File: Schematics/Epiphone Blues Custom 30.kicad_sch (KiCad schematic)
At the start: 274 parts, among them J3 Conn_Coaxial_Power, M1 Fan, SW2 EQ mode, SW3 POWER, SW4 STANDBY, SW5 PENTODE

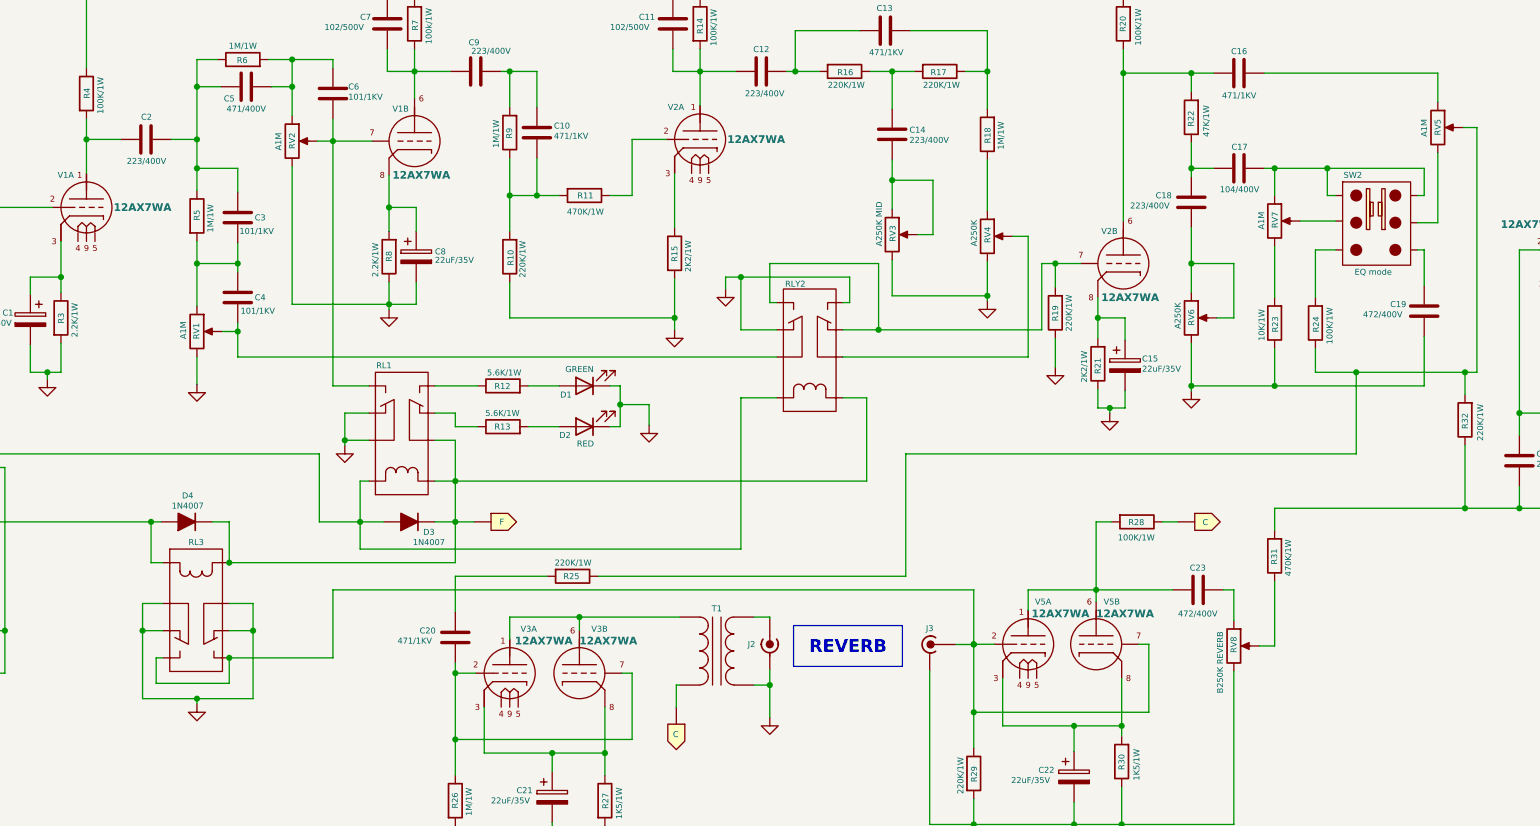
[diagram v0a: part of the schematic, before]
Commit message: Added text to schematic
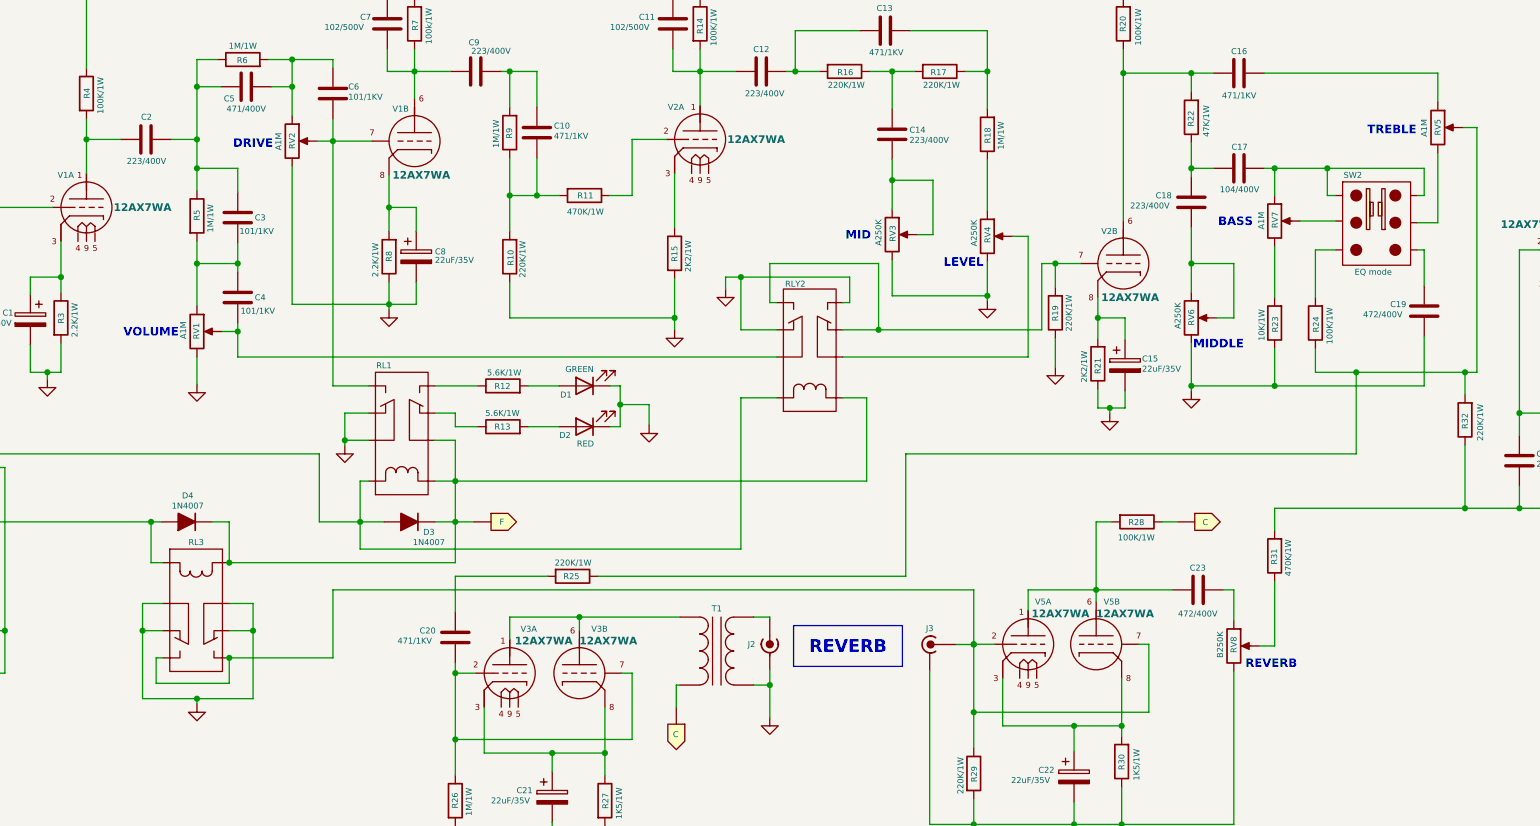
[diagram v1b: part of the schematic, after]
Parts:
- RV3: value A250K MID -> A250K
- RV8: value B250K REVERB -> B250K
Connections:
- net at FCR.: now also B., C33.1, R49.1; no longer TRF4.
- net at SS1.: now also F4.1; no longer SW4.
- net at 0VAC.: now also TR2.; no longer PT3.
- net at 60VAC.: now also TR2.; no longer PT11.
- net at PT2.: now also PT3., PT6. (x2)
- net at V7.: now also C29.1, R44.2, V6.
- net at PT5.: now also PT6. (x2)
- net at PT6.: no longer PT5. (x2)
- net at PT4.: now also PT1., PT7.
- net at ff.: now also BLUE.; no longer TR3.
- net at BLUE.: now also OT6.; no longer ff.
- net at PT7.: now also PT1.
- net at PT1.: no longer PT7.
- net at U?.: now also OUT1.; no longer TR3.
- net at OUT1.: now also PS1., V6.; no longer U?.
- net at 120VAC.: now also TR2.; no longer PT5.
- net at TR3.: now also d.; no longer d.
- net at a.: now also d.; no longer TR3.
- net at s.: now also d.; no longer TR3.
- net at d.: now also s.; no longer TR3.
- net at PT7.: now also 100VAC.
- net at 100VAC.: now also TR2.; no longer PT7.
- net at 5VAC.: now also PT13.
- net at PT13.: now also C35.1, HTFS., R50.1, V8.; no longer 5VAC.
- net at BLK.: now also SW3.; no longer PT1.
- net at SW3.: now also BLU.; no longer BLK.
- net at 0VAC.: now also TR2.; no longer PT6.
- net at 100VAC.: now also TR2.; no longer PT4.
- net at V6., V7.: now also PT15.; no longer PT14.
- net at PT1.: now also PT8.
- net at PT8.: no longer PT1.
- net at SW2.: now also RV7.; no longer RV5.
- net at RV7.: now also R23.2; no longer SW2.
- net at 120VAC.: now also TR2.; no longer PT8.
- net at SW4.: now also 350VAC.; no longer 350VAC.
- net at 350VAC.: now also TR2.; no longer SW4.
- net at PT2.: now also PT3.
- net at PT3.: no longer PT2.
- net at PT5.: now also PT1., PT8.
- net at 0VAC.: now also PT12.
- net at PT12.: now also F7.1; no longer 0VAC.
- net at s.: now also a.; no longer d.
- net at a.: now also J6., J7.; no longer s.
- net at BRN.: now also F9.2; no longer SW3.
- net at BLU.: now also AC-Input1.; no longer SW3.
- net at PT3.: now also PT2.
- net at PT2.: no longer PT3.
- new net: C3.1, D6.1 (K), D7.1 (K), F., M1. (-), V1., V2., V3., V4., V5.
- new net: FCR., TRF4.
- new net: SS1., SW4.
- new net: 0VAC., PT3.
- new net: 0VAC., TR2. (x2)
- new net: D4.2 (A), J4., RL3.
- new net: D3.2 (A), J4., RL1., RLY2.
- new net: J4., PB1.
- new net: 60VAC., PT11.
- new net: J3. (In), R29.1, RL3., V5A., V5B.
- new net: OUT2., PS2., V7.
- new net: TR3., ff.
- new net: TR3., U?.
- new net: B., PS5., PS6.
- new net: J5., J6., J7., J8., J9., d.
- new net: C4.2, RLY2., RV1.
- new net: 120VAC., PT5.
- new net: R19.2, RLY2., V2B.
- new net: RLY2., RV4.
- new net: TR3., d.
- new net: TR3., a.
- new net: TR3., s.
- new net: BLK., PT1.
- new net: 0VAC., PT6.
- new net: 100VAC., PT4.
- new net: PT14., V6., V7.
- new net: C17.2, RV7., SW2.
- new net: RV5., SW2.
- new net: 120VAC., PT8.
- new net: 350VAC., SW4.
- new net: C6.2, RL1., RV2., V1B.
- new net: BRN., SW3.
- new net: J2. (In), T1. (SB)
- now unconnected: PT1., PT1., PT3., PT3., PT6., PT6., PT7., PT8., V6., V6.
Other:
- note added: "BASS"
- note added: "DRIVE"
- note added: "LEVEL"
- note added: "MID"
- note added: "MIDDLE"
- note added: "TREBLE"
- note added: "VOLUME"
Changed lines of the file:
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@@
 		)
 	)
+	(text "TREBLE"
+		(exclude_from_sim no)
+		(at 281.178 44.958 0)
+		(effects
+			(font
+				(size 1.27 1.27)
+				(thickness 0.254)
+				(bold yes)
+				(color 0 132 0 1)
+			)
+		)
+	)
+	(text "MID"
+		(exclude_from_sim no)
+		(at 201.422 60.706 0)
+		(effects
+			(font
+				(size 1.27 1.27)
+				(thickness 0.254)
+				(bold yes)
+				(color 0 132 0 1)
+			)
+		)
+	)
 	(text "RED"
 		(exclude_from_sim no)
@@
 		)
 	)
+	(text "DRIVE"
+		(exclude_from_sim no)
+		(at 110.998 46.99 0)
+		(effects
+			(font
+				(size 1.27 1.27)
+				(thickness 0.254)
+				(bold yes)
+				(color 0 132 0 1)
+			)
+		)
+	)
 	(text "BRN"
 		(exclude_from_sim no)
@@
 		)
 	)
+	(text "MIDDLE"
+		(exclude_from_sim no)
+		(at 255.27 76.962 0)
+		(effects
+			(font
+				(size 1.27 1.27)
+				(thickness 0.254)
+				(bold yes)
+				(color 0 132 0 1)
+			)
+		)
+	)
 	(text "MAIN FUSE\n100-120VAC T3.15AL 250V\n220-240VAC T1.6AL 250V"
 		(exclude_from_sim no)
@@
 		)
 	)
+	(text "VOLUME"
+		(exclude_from_sim no)
+		(at 95.758 75.184 0)
+		(effects
+			(font
+				(size 1.27 1.27)
+				(thickness 0.254)
+				(bold yes)
+				(color 0 132 0 1)
+			)
+		)
+	)
 	(text "BLU"
 		(exclude_from_sim no)
@@
 		)
 	)
+	(text "BASS"
+		(exclude_from_sim no)
+		(at 257.81 58.674 0)
+		(effects
+			(font
+				(size 1.27 1.27)
+				(thickness 0.254)
+				(bold yes)
+				(color 0 132 0 1)
+			)
+		)
+	)
 	(text "@250mA"
 		(exclude_from_sim no)
@@
 		)
 	)
+	(text "REVERB"
+		(exclude_from_sim no)
+		(at 263.144 124.714 0)
+		(effects
+			(font
+				(size 1.27 1.27)
+				(thickness 0.254)
+				(bold yes)
+				(color 0 132 0 1)
+			)
+		)
+	)
 	(text "BLK"
 		(exclude_from_sim no)
@@
 		)
 	)
+	(text "LEVEL"
+		(exclude_from_sim no)
+		(at 217.17 64.77 0)
+		(effects
+			(font
+				(size 1.27 1.27)
+				(thickness 0.254)
+				(bold yes)
+				(color 0 132 0 1)
+			)
+		)
+	)
 	(text "RED"
 		(exclude_from_sim no)
@@
 	)
 	(symbol
-		(lib_name "Epi-BC-30:12AX7a")
 		(lib_id "Epi-BC-30:12AX7a")
 		(at 308.356 62.738 0)
@@
 	)
 	(symbol
-		(lib_name "Epi-BC-30:Label")
 		(lib_id "Epi-BC-30:Label")
 		(at 198.628 237.744 180)
@@
 	)
 	(symbol
-		(lib_name "Epi-BC-30:5881")
 		(lib_id "Epi-BC-30:5881")
 		(at 312.42 189.992 0)
@@
 	)
 	(symbol
-		(lib_name "Epi-BC-30:Label")
 		(lib_id "Epi-BC-30:Label")
 		(at 252.476 166.37 0)
@@
 	)
 	(symbol
-		(lib_name "Epi-BC-30:12AX7a")
 		(lib_id "Epi-BC-30:12AX7a")
 		(at 149.352 125.984 0)
@@
 			)
 		)
-		(property "Value" "B250K REVERB"
+		(property "Value" "B250K"
 			(at 255.5156 119.743 90)
 			(effects
@@
 	)
 	(symbol
-		(lib_name "Epi-BC-30:Label")
 		(lib_id "Epi-BC-30:Label")
 		(at 174.752 258.064 180)
@@
 	)
 	(symbol
-		(lib_name "Epi-BC-30:12AX7a")
 		(lib_id "Epi-BC-30:12AX7a")
 		(at 177.8 46.228 0)
@@
 	)
 	(symbol
-		(lib_name "Epi-BC-30:Label")
 		(lib_id "Epi-BC-30:Label")
 		(at 252.476 174.498 0)
@@
 	)
 	(symbol
-		(lib_name "Epi-BC-30:Label")
 		(lib_id "Epi-BC-30:Label")
 		(at 228.6 182.626 0)
@@
 	)
 	(symbol
-		(lib_name "Epi-BC-30:Label")
 		(lib_id "Epi-BC-30:Label")
 		(at 174.752 215.392 180)
@@
 	)
 	(symbol
-		(lib_name "Epi-BC-30:Label")
 		(lib_id "Epi-BC-30:Label")
 		(at 174.752 264.16 180)
@@
 	)
 	(symbol
-		(lib_name "Epi-BC-30:Label")
 		(lib_id "Epi-BC-30:Label")
 		(at 198.628 254 180)
@@
 	)
 	(symbol
-		(lib_name "Epi-BC-30:Label")
 		(lib_id "Epi-BC-30:Label")
 		(at 198.628 245.872 180)
@@
 	)
 	(symbol
-		(lib_name "Epi-BC-30:Label")
 		(lib_id "Epi-BC-30:Label")
 		(at 252.476 182.626 0)
@@
 	)
 	(symbol
-		(lib_name "Epi-BC-30:Label")
 		(lib_id "Epi-BC-30:Label")
 		(at 174.752 229.616 180)
@@
 	)
 	(symbol
-		(lib_name "Epi-BC-30:5881")
 		(lib_id "Epi-BC-30:5881")
 		(at 312.42 159.512 0)
@@
 	)
 	(symbol
-		(lib_name "Epi-BC-30:Label")
 		(lib_id "Epi-BC-30:Label")
 		(at 174.752 219.456 180)
@@
 	)
 	(symbol
-		(lib_name "Epi-BC-30:12AX7a")
 		(lib_id "Epi-BC-30:12AX7a")
 		(at 226.822 121.666 0)
@@
 			)
 		)
-		(property "Value" "A250K MID"
-			(at 204.5617 55.5022 90)
+		(property "Value" "A250K"
+			(at 204.47 58.166 90)
 			(effects
 				(font

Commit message: new branch for Version 2006 Modifications
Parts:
- C1: value 4.7uF/50V -> 22uF/50V
- C10: value 471/1KV -> 101/1KV
- C25, C26: value 223/400V -> 104/400V
- C3: value 101/1KV -> 471/1KV
- C5: value 471/400V -> 100/400V
- R17: value 220K/1W -> 470K/1W
- R19, R39: value 220K/1W -> 1M/1W
- R23: value 10K/1W -> 5K6/1W
- R3, R8: value 2.2K/1W -> 1K5/1W
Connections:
- net at FCR.: now also B., C33.1, R49.1; no longer TRF4.
- net at SS1.: now also F4.1; no longer SW4.
- net at 0VAC.: now also TR2.; no longer PT3.
- net at 60VAC.: now also TR2.; no longer PT11.
- net at PT2.: now also PT3., PT6. (x2)
- net at V7.: now also C29.1, R44.2, V6.
- net at PT5.: now also PT6. (x2)
- net at PT6.: no longer PT5. (x2)
- net at PT4.: now also PT1., PT7.
- net at ff.: now also BLUE.; no longer TR3.
- net at BLUE.: now also OT6.; no longer ff.
- net at PT7.: now also PT1.
- net at PT1.: no longer PT7.
- net at U?.: now also OUT1.; no longer TR3.
- net at OUT1.: now also PS1., V6.; no longer U?.
- net at 120VAC.: now also TR2.; no longer PT5.
- net at TR3.: now also d.; no longer d.
- net at a.: now also d.; no longer TR3.
- net at s.: now also d.; no longer TR3.
- net at d.: now also s.; no longer TR3.
- net at PT7.: now also 100VAC.
- net at 100VAC.: now also TR2.; no longer PT7.
- net at 5VAC.: now also PT13.
- net at PT13.: now also C35.1, HTFS., R50.1, V8.; no longer 5VAC.
- net at BLK.: now also SW3.; no longer PT1.
- net at SW3.: now also BLU.; no longer BLK.
- net at 0VAC.: now also TR2.; no longer PT6.
- net at 100VAC.: now also TR2.; no longer PT4.
- net at V6., V7.: now also PT15.; no longer PT14.
- net at PT1.: now also PT8.
- net at PT8.: no longer PT1.
- net at SW2.: now also RV7.; no longer RV5.
- net at RV7.: now also R23.2; no longer SW2.
- net at 120VAC.: now also TR2.; no longer PT8.
- net at SW4.: now also 350VAC.; no longer 350VAC.
- net at 350VAC.: now also TR2.; no longer SW4.
- net at PT2.: now also PT3.
- net at PT3.: no longer PT2.
- net at PT5.: now also PT1., PT8.
- net at 0VAC.: now also PT12.
- net at PT12.: now also F7.1; no longer 0VAC.
- net at s.: now also a.; no longer d.
- net at a.: now also J6., J7.; no longer s.
- net at BRN.: now also F9.2; no longer SW3.
- net at BLU.: now also AC-Input1.; no longer SW3.
- net at PT3.: now also PT2.
- net at PT2.: no longer PT3.
- new net: C3.1, D6.1 (K), D7.1 (K), F., M1. (-), V1., V2., V3., V4., V5.
- new net: FCR., TRF4.
- new net: SS1., SW4.
- new net: 0VAC., PT3.
- new net: 0VAC., TR2. (x2)
- new net: D4.2 (A), J4., RL3.
- new net: D3.2 (A), J4., RL1., RLY2.
- new net: J4., PB1.
- new net: 60VAC., PT11.
- new net: J3. (In), R29.1, RL3., V5A., V5B.
- new net: OUT2., PS2., V7.
- new net: TR3., ff.
- new net: TR3., U?.
- new net: B., PS5., PS6.
- new net: J5., J6., J7., J8., J9., d.
- new net: C4.2, RLY2., RV1.
- new net: 120VAC., PT5.
- new net: R19.2, RLY2., V2B.
- new net: RLY2., RV4.
- new net: TR3., d.
- new net: TR3., a.
- new net: TR3., s.
- new net: BLK., PT1.
- new net: 0VAC., PT6.
- new net: 100VAC., PT4.
- new net: PT14., V6., V7.
- new net: C17.2, RV7., SW2.
- new net: RV5., SW2.
- new net: 120VAC., PT8.
- new net: 350VAC., SW4.
- new net: C6.2, RL1., RV2., V1B.
- new net: BRN., SW3.
- new net: J2. (In), T1. (SB)
- now unconnected: PT1., PT1., PT3., PT3., PT6., PT6., PT7., PT8., V6., V6.
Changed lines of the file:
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@@
 			)
 		)
-		(property "Value" "223/400V"
+		(property "Value" "104/400V"
 			(at 329.7623 49.1923 90)
 			(effects
@@
 			)
 		)
-		(property "Value" "471/400V"
+		(property "Value" "100/400V"
 			(at 109.982 41.656 90)
 			(effects
@@
 			)
 		)
-		(property "Value" "223/400V"
+		(property "Value" "104/400V"
 			(at 329.7623 45.7405 90)
 			(effects
@@
 			)
 		)
-		(property "Value" "2.2K/1W"
+		(property "Value" "1K5/1W"
 			(at 84.3554 75.7844 90)
 			(effects
@@
 			)
 		)
-		(property "Value" "101/1KV"
+		(property "Value" "471/1KV"
 			(at 108.966 59.944 0)
 			(effects
@@
 			)
 		)
-		(property "Value" "220K/1W"
-			(at 232.918 74.93 90)
+		(property "Value" "1M/1W"
+			(at 232.918 74.422 90)
 			(effects
 				(font
@@
 			)
 		)
-		(property "Value" "2.2K/1W"
-			(at 129.286 66.802 90)
+		(property "Value" "1K5/1W"
+			(at 129.286 66.548 90)
 			(effects
 				(font
@@
 			)
 		)
-		(property "Value" "471/1KV"
+		(property "Value" "101/1KV"
 			(at 155.956 45.72 0)
 			(effects
@@
 			)
 		)
-		(property "Value" "10K/1W"
+		(property "Value" "5K6/1W"
 			(at 261.7204 76.3352 90)
 			(effects
@@
 			)
 		)
-		(property "Value" "220K/1W"
+		(property "Value" "1M/1W"
 			(at 307.6104 103.6247 90)
 			(effects
@@
 			)
 		)
-		(property "Value" "4.7uF/50V"
+		(property "Value" "22uF/50V"
 			(at 74.93 73.66 0)
 			(effects
@@
 			)
 		)
-		(property "Value" "220K/1W"
+		(property "Value" "470K/1W"
 			(at 213.868 38.1 90)
 			(effects
